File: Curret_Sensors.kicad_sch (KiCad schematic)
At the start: 15 parts, among them U1 INA282, U2 INA282, U3 INA282

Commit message: VER2.0
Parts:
- added R3, R5, R7: 0.5m, Resistor_SMD:R_2512_6332Metric_Pad1.40x3.35mm_HandSolder, symbol Device:R
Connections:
- net +3.3V renamed +3.3VA
- net A renamed A-
- net A-: now also R3.1
- net A_OUT renamed A+
- net A+: now also R3.2
- net B renamed B+
- net B+: now also R5.2
- net B_OUT renamed B-
- net B-: now also R5.1
- net C renamed C+
- net C+: now also R7.2
- net C_OUT renamed C-
- net C-: now also R7.1
- net GND renamed GNDA

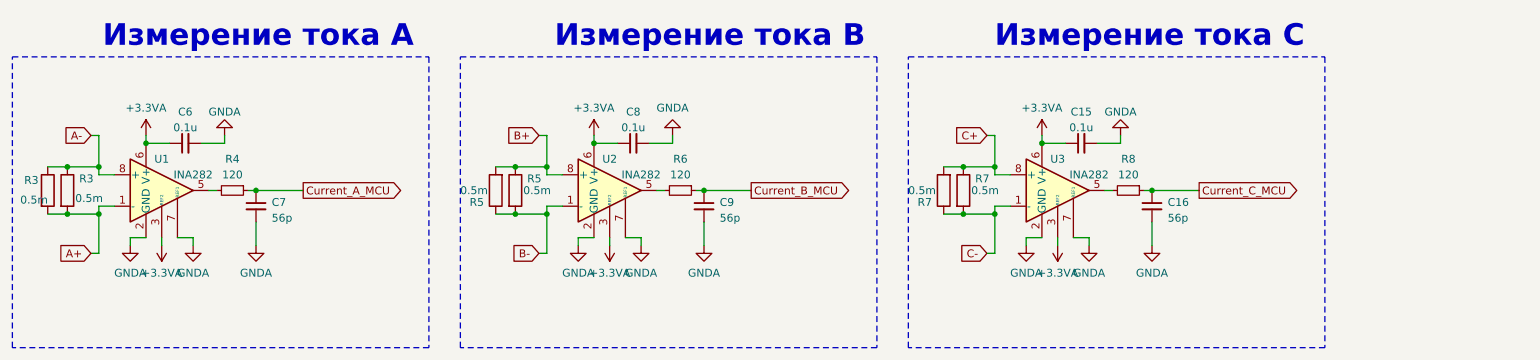
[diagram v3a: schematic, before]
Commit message: Убрал лишние шунты
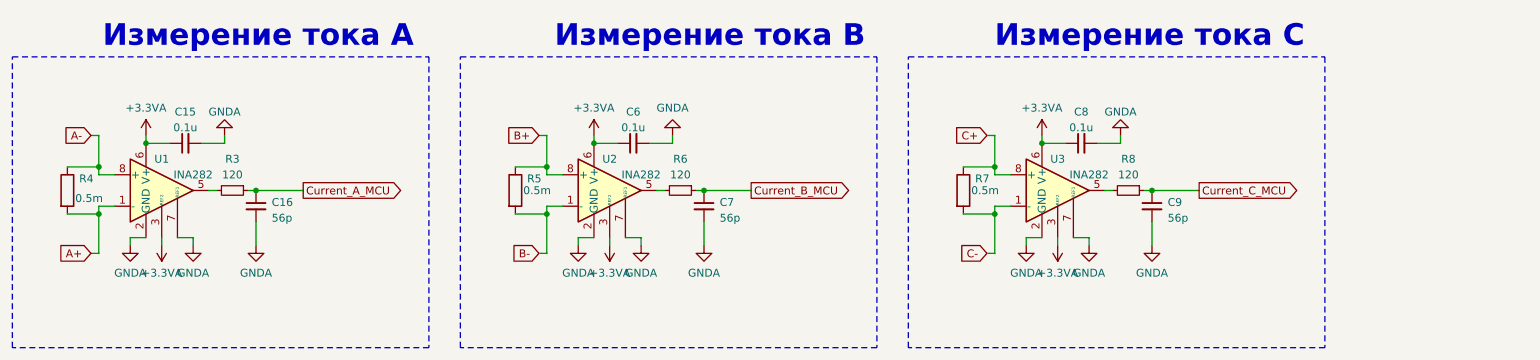
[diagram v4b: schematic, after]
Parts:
- removed R3, R5, R7: 0.5m, Resistor_SMD:R_2512_6332Metric_Pad1.40x3.35mm_HandSolder, symbol Device:R
- renumbered C6 to C15, C7 to C16, C8 to C6, C9 to C7, C15 to C8, C16 to C9, R4 to R3, R3 to R4
